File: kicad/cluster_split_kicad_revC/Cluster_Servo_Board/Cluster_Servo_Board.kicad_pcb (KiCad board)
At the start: 4 copper layers, 220 x 110 mm, 34 parts, among them J1 JST_XH_8, J10 POWER_5V_HICUR, J11 POWER_5V_HICUR, J2 RJ45_Amphenol_54602-x08_Horiz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, J3 RJ45_Amphenol_54602-x08_Horiz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, J4 RJ45_Amphenol_54602-x08_Horiz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, J5 RJ45_Amphenol_54602-x08_Horiz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, J6 RJ45_Amphenol_54602-x08_Horiz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, J7 RJ45_Amphenol_54602-x08_Horiz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, J8 RJ45_Amphenol_54602-x08_Horiz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, J9 RJ45_Amphenol_54602-x08_Horiz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, U1 ADAFRUIT_PCA9685_16CH_PRODUCT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, U2 74AHCT125_DIP14

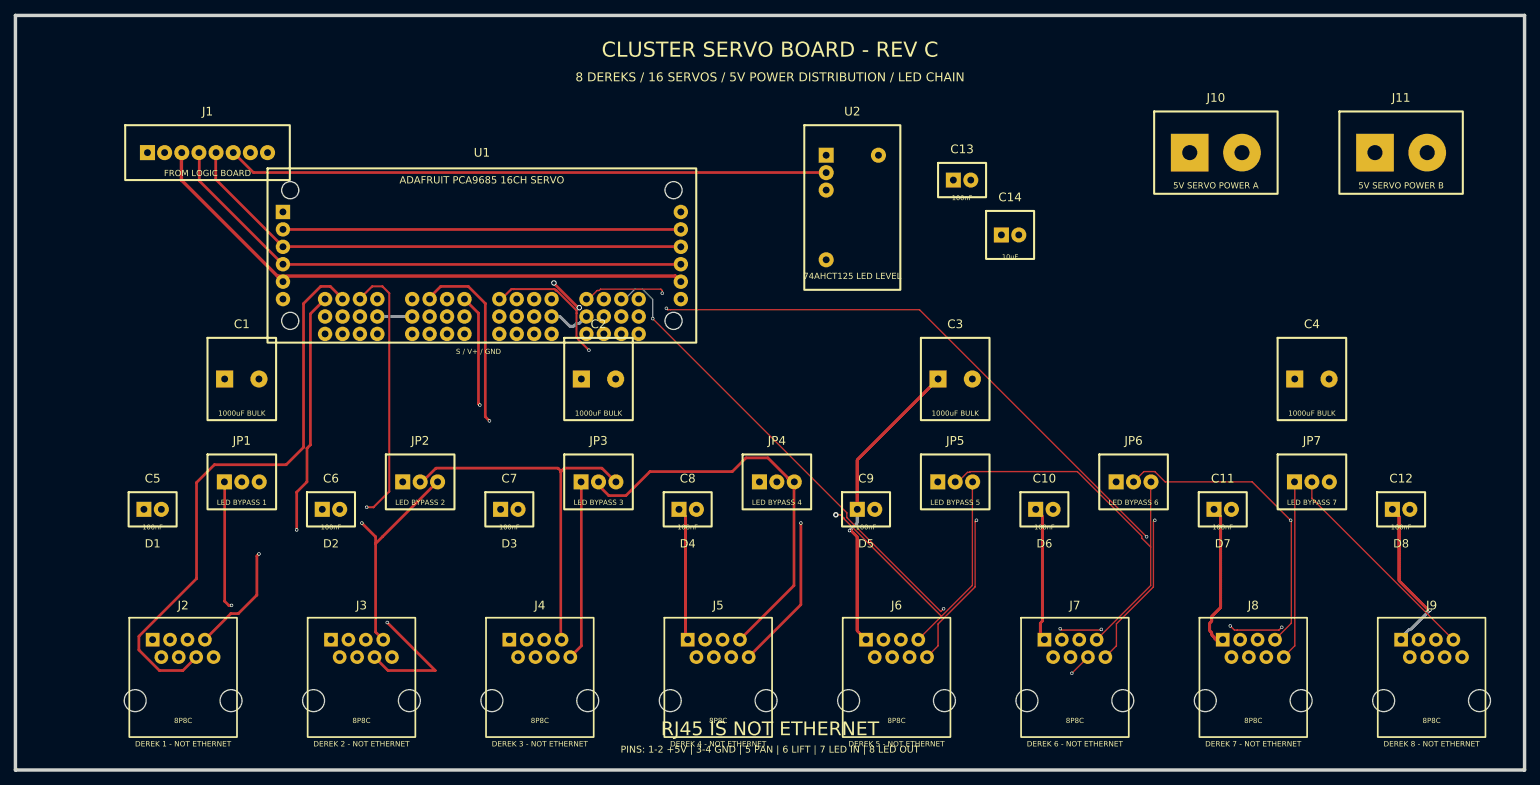
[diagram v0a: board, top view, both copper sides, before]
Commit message: Servo Controller board routed and passes DRC
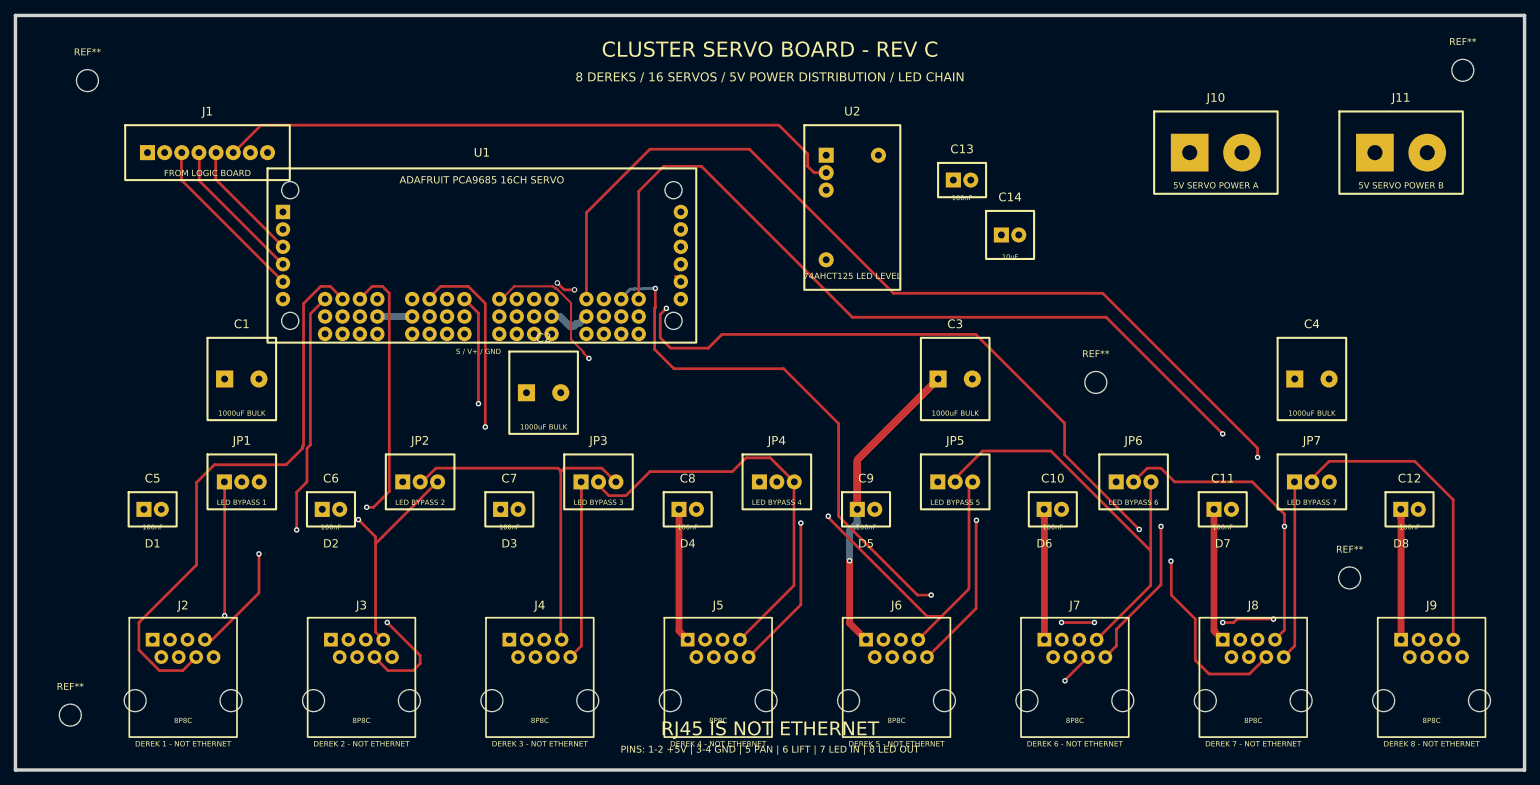
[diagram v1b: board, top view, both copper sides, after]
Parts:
- added REF**: MountingHole_3.2mm_M3, MountingHole:MountingHole_3.2mm_M3, F.Cu at (194.5, 82.0)
- added REF**: MountingHole_3.2mm_M3, MountingHole:MountingHole_3.2mm_M3, F.Cu at (211.0, 8.00)
- added REF**: MountingHole_3.2mm_M3, MountingHole:MountingHole_3.2mm_M3, F.Cu at (10.5, 9.50)
- added REF**: MountingHole_3.2mm_M3, MountingHole:MountingHole_3.2mm_M3, F.Cu at (8.00, 102.0)
- added REF**: MountingHole_3.2mm_M3, MountingHole:MountingHole_3.2mm_M3, F.Cu at (157.5, 53.5)
- moved C2 8.25 mm to (77.0, 55.0)
- moved C10 1.23 mm to (151.2, 72.0)
- moved C12 1.23 mm to (203.2, 72.0)
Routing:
- net PWM15: track 141.8 -> 192.4 mm, vias 0 -> 1
- net PWM12: track 130.2 -> 160.2 mm
- net LED_IN8: track 31.5 -> 44.9 mm
- net PWM14: track 146.6 -> 159.9 mm
- net PWM9: track 96.5 -> 109.7 mm
- net PWM13: track 124.4 -> 136.2 mm, vias 2 -> 3
- net +5V_SERVO: track 140.1 -> 132.6 mm, vias 2 -> 1
- net LED_DATA_3V3: track 87.6 -> 92.1 mm
- net PWM3: track 68.4 -> 64.7 mm
- net LED_IN6: track 59.7 -> 62.8 mm
- net PWM10: track 101.9 -> 104.5 mm
- net PWM11: track 105.9 -> 107.9 mm
- net +3V3_LOGIC: track 82.9 -> 84.8 mm
- net LED_OUT1: track 27.2 -> 26.2 mm
- net I2C_SDA: track 79.4 -> 80.4 mm
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- removed copper zone on In1.Cu, net +5V_SERVO
